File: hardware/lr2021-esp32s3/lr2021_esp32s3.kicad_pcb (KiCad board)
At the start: 4 copper layers, 90 x 65 mm, 84 parts, among them J1 USB-C, J2 5V IN, J3 3V3 IN, J4 GPIO, J5 SMA 915MHz, J6 SMA 2.4GHz, SW1 RESET, SW2 BOOT, U1 USBLC6-2SC6, U2 AP7361C-33E, U3 LM66100, U4 LM66100, U5 ESP32-S3-WROOM-1-N16R8, U6 LR2021IMLTRT, Y1 32MHz

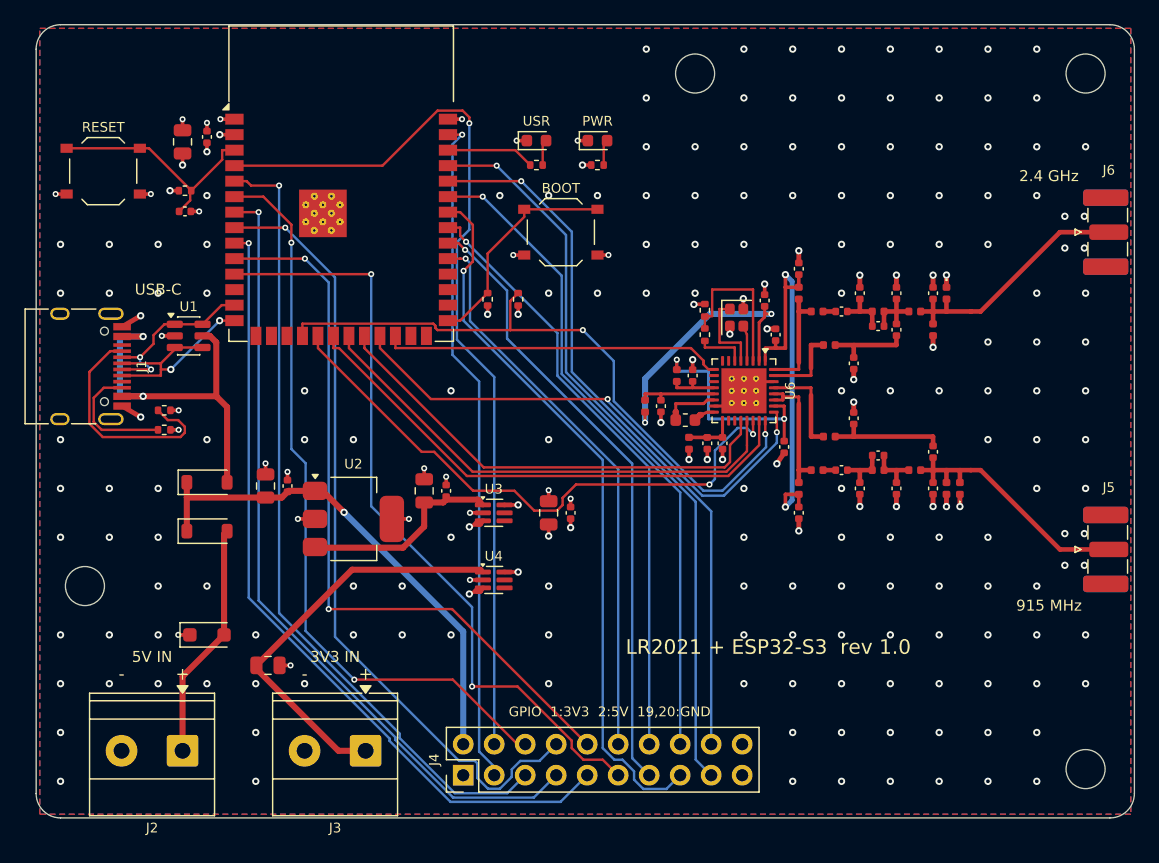
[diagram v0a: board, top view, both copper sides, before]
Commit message: Fix screw terminal orientation: wire entry now faces the board edge
J2/J3 were placed at 180 deg, which pointed the wire openings into the
board (confirmed in the 3D view). They are now at 0 deg with the body
front 0.2 mm inside the edge; +/- silkscreen moved with pin 1 (left pad).
Board re-routed and re-exported (DRC: 0 errors, 0 unconnected, parity OK).

Co-Authored-By: Claude Opus 5.5 <noreply@anthropic.com>
Claude-Session: https://claude.ai/code/session_01GybN5CQfdUnddB4A81xgKu
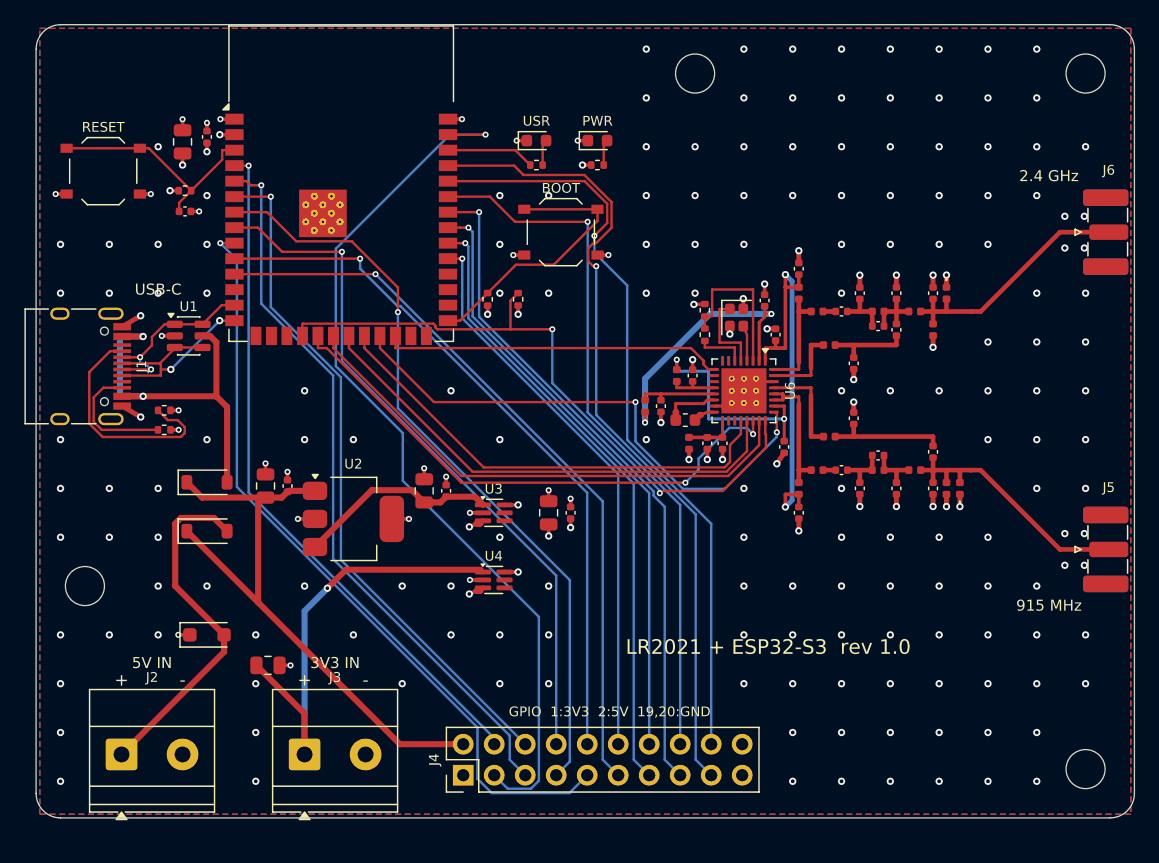
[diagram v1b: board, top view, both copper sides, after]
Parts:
- moved J2 5.01 mm to (107.0, 159.8), turned to 0 degrees
- moved J3 5.01 mm to (122.0, 159.8), turned to 0 degrees
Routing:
- net /GPIO1: track 55.4 -> 74.1 mm
- net /GPIO4: track 74.4 -> 56.9 mm
- net /+5V_EXT: track 19.5 -> 29.0 mm
- net +5V: track 40.9 -> 49.7 mm, vias 1 -> 0
- net /GPIO15: track 65.2 -> 57.3 mm
- net /GPIO5: track 66.0 -> 59.6 mm
- net /U0TXD: track 61.2 -> 66.8 mm
- net /GPIO6: track 61.2 -> 56.5 mm, vias 2 -> 1
- net /BOOT: track 18.3 -> 22.6 mm
- net /U0RXD: track 58.6 -> 62.5 mm
- net /GPIO42: track 54.4 -> 58.3 mm
- net /GPIO7: track 65.8 -> 62.2 mm
- net /GPIO41: track 59.0 -> 55.5 mm
- net /GPIO17: track 61.1 -> 57.9 mm, vias 2 -> 1
- net /LR_MOSI: track 48.0 -> 44.9 mm
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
